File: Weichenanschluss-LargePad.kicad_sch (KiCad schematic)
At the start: 36 parts, among them J1 A1.1, J1001 Conn_01x01, J11 +V, J12 fb1, J13 fb2, J2 A1.2, J22 Za, J23 H, J25 g, J26 a, J27 Tg, J28 Ta, J29 GND, J3 Aux1, J30 GND, J31 +12, J32 Rü1, J33 Rü2, J4 Aux2, J41 g, J42 a, J43 +12V, J44 GND, J5 A2.1, J51 g, J52 a, J53 +12V, J54 GND, J6 A2.2, J7 Prz1, J8 Prz2, J9 -V, U1001 ULN2803A

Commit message: Kicad 10
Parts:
- added BT1001: 12V, symbol Device:Battery
- added J1001, J1006: Zg, symbol Connector:Conn_01x01_Pin
- added J1002, J1007: Za, symbol Connector:Conn_01x01_Pin
- added J1003: ZH, symbol Connector:Conn_01x01_Pin
- added J1004: g, symbol Connector:Conn_01x01_Pin
- added J1005: a, symbol Connector:Conn_01x01_Pin
- added J1008, J1012, J1013, J1014: H, symbol Connector:Conn_01x01_Pin
- added J1009: Poz1, symbol Connector:Conn_01x01_Pin
- added J1010, J1015: +V, symbol Connector:Conn_01x01_Pin
- added J1011: Poz2, symbol Connector:Conn_01x01_Pin
- added J1016, J1017: fb2, symbol Connector:Conn_01x01_Pin
- J21: renamed from J1001; value Conn_01x01 -> Zg
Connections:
- net +12V: now also BT1001.1 (+), J1010.1 (Pin_1)
- net GND: now also BT1001.2 (-)
- net at J13.1 (Pin_1), J33.1 (Pin_1): now also J1017.1 (Pin_1)
- net at J26.1 (Pin_1), J42.1 (Pin_1), J52.1 (Pin_1)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: now also J1005.1 (Pin_1), J1014.1 (Pin_1)
- net at J12.1 (Pin_1), J32.1 (Pin_1): now also J1016.1 (Pin_1)
- net at J27.1 (Pin_1), J7.1 (Pin_1), U1001.18 (O1): now also J1009.1 (Pin_1)
- net at J1.1 (Pin_1), J21.1 (Pin_1): now also J1001.1 (Pin_1), J1006.1 (Pin_1)
- net at J23.1 (Pin_1), J3.1 (Pin_1), J4.1 (Pin_1): now also J1003.1 (Pin_1), J1012.1 (Pin_1)
- net at J25.1 (Pin_1), J41.1 (Pin_1), J5.1 (Pin_1)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: now also J1004.1 (Pin_1), J1013.1 (Pin_1)
- net at J28.1 (Pin_1), J8.1 (Pin_1), U1001.17 (O2): now also J1011.1 (Pin_1)
- net at J2.1 (Pin_1), J22.1 (Pin_1): now also J1002.1 (Pin_1), J1007.1 (Pin_1)
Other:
- moved on the sheet: J1, J11, J12, J13, J2, J21, J22, J23, J25, J26, J27, J28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

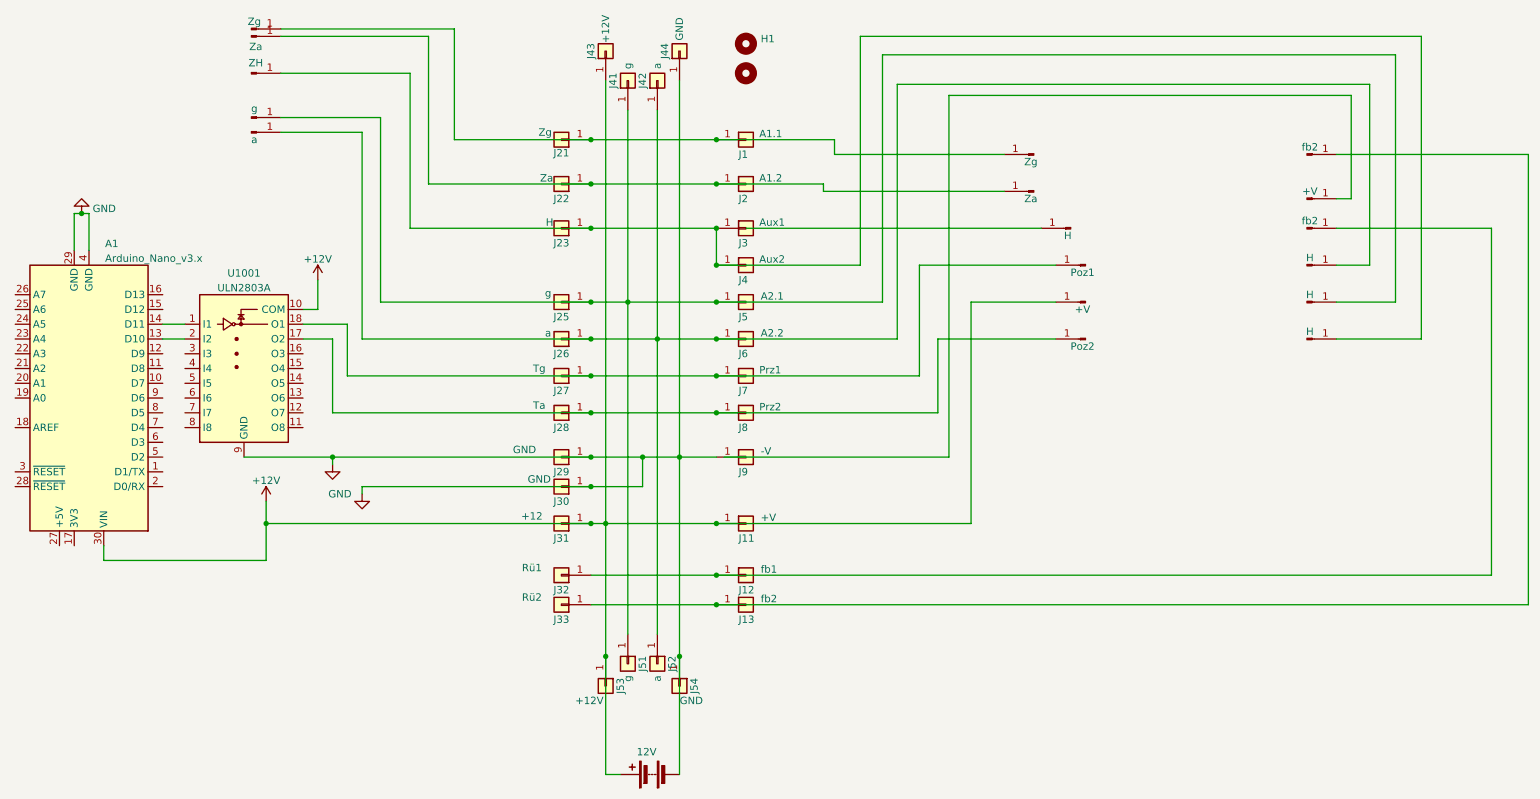
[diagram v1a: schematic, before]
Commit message: Name der Pad-Footprints angepasst: Wago->Connector_Misc
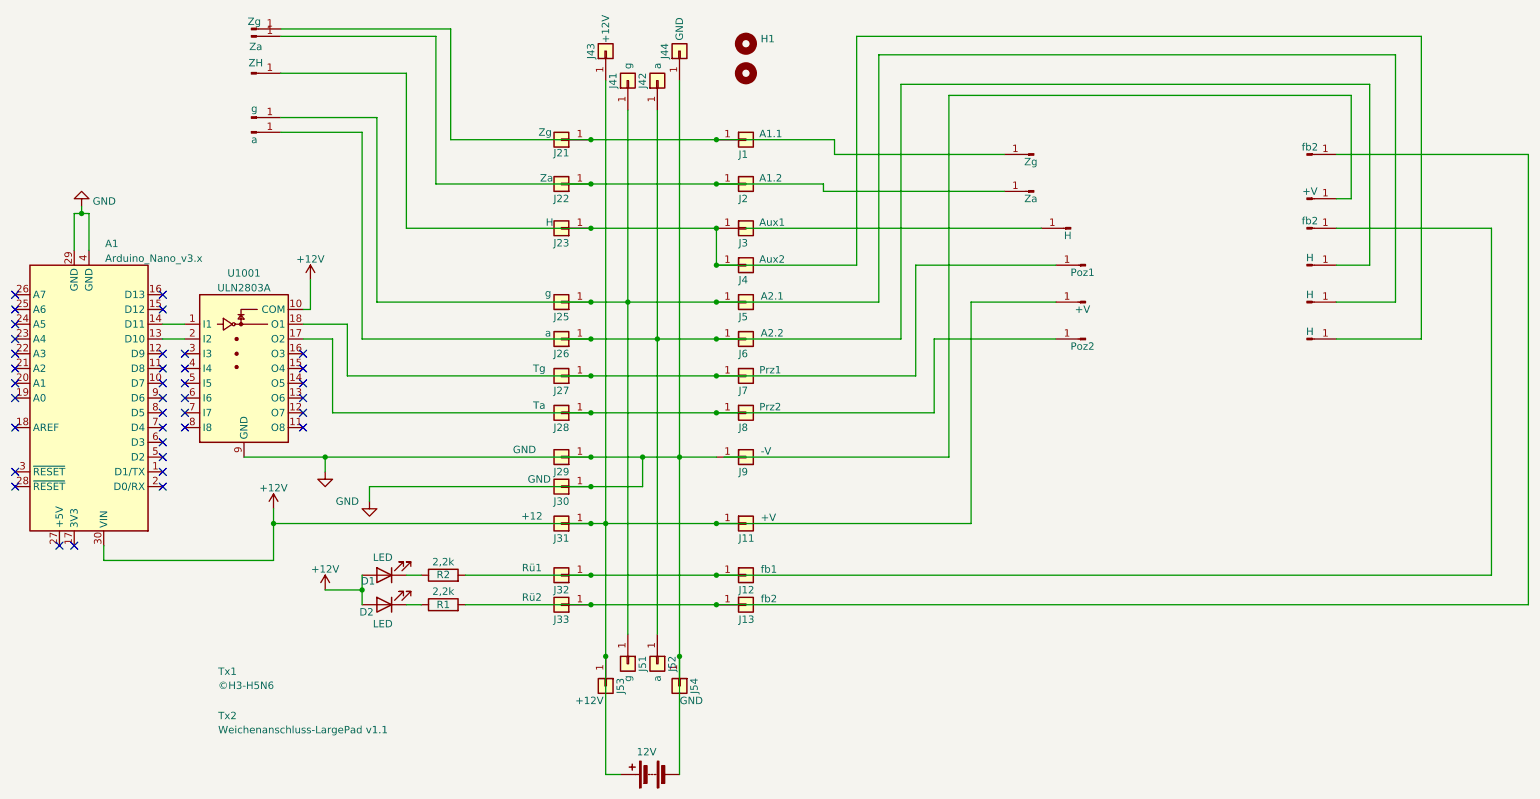
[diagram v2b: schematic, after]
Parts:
- added D1, D2: LED, symbol Device:LED
- added R1, R2: 2,2k, symbol Device:R
- added Tx1: ©H3-H5N6, Text:Text, symbol Text:Text
- added Tx2: ${TITLE} ${REVISION}, Text:Text, symbol Text:Text
- J1, J11, J12, J13, J2, J21, J22, J23, J25, J26, J27, J28, J29, J3, J30, J31, J32, J33, J4, J41, J42, J43, J44, J5, J51, J52, J53, J54, J6, J7, J8, J9: footprint Wago:Pad_7.5x2.2mm -> Connector_Misc:Pad_7.5x2.2mm
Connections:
- net +12V: now also D1.2 (A), D2.2 (A)
- net at J1017.1 (Pin_1), J13.1 (Pin_1), J33.1 (Pin_1): now also R2.2
- net at J1016.1 (Pin_1), J12.1 (Pin_1), J32.1 (Pin_1): now also R1.2
- new net: D1.1 (K), R1.1
- new net: D2.1 (K), R2.1
- no-connect marks 0 -> 37
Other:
- title: (none) -> Weichenanschluss-LargePad
